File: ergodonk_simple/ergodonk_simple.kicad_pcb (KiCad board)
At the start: 2 copper layers, 216.6 x 155.6 mm, 134 parts, among them J10 Pimaroni Trackball, J11 4PIN, Q1 TIP120, SW0 SW_PUSH_LED, SW08_RH10 SW_PUSH_LED, SW1 SW_PUSH_LED, SW10 SW_PUSH_LED, SW11 SW_PUSH_LED, SW12 SW_PUSH_LED, SW13 SW_PUSH_LED, SW14 SW_PUSH_LED, SW15 SW_PUSH_LED, SW16 SW_PUSH_LED, SW17 SW_PUSH_LED, SW18_RH10 SW_PUSH_LED, SW2 SW_PUSH_LED, SW20 SW_PUSH_LED, SW21 SW_PUSH_LED, SW22 SW_PUSH_LED, SW23 SW_PUSH_LED, SW24 SW_PUSH_LED, SW25 SW_PUSH_LED, SW26 SW_PUSH_LED, SW27 SW_PUSH_LED, SW28_RH10 SW_PUSH_LED, SW3 SW_PUSH_LED, SW30 SW_PUSH_LED, SW31 SW_PUSH_LED, SW32 SW_PUSH_LED, SW33 SW_PUSH_LED, SW34 SW_PUSH_LED, SW35 SW_PUSH_LED, SW36 SW_PUSH_LED, SW37 SW_PUSH_LED, SW38_RH10 SW_PUSH_LED, SW4 SW_PUSH_LED, SW40 SW_PUSH_LED, SW42 SW_PUSH_LED, SW43 SW_PUSH_LED, SW44 SW_PUSH_LED, SW45 SW_PUSH_LED, SW46 SW_PUSH_LED, SW47 SW_PUSH_LED, SW48_RH10 SW_PUSH_LED, SW5 SW_PUSH_LED, SW50 SW_PUSH_LED, SW51 SW_PUSH_LED, SW52 SW_PUSH_LED, SW53 SW_PUSH_LED, SW54 SW_PUSH_LED, SW55 SW_PUSH_LED, SW56 SW_PUSH_LED, SW57 SW_PUSH_LED, SW58 SW_PUSH_LED, SW6 SW_PUSH_LED, SW7 SW_PUSH_LED, U11 Pico

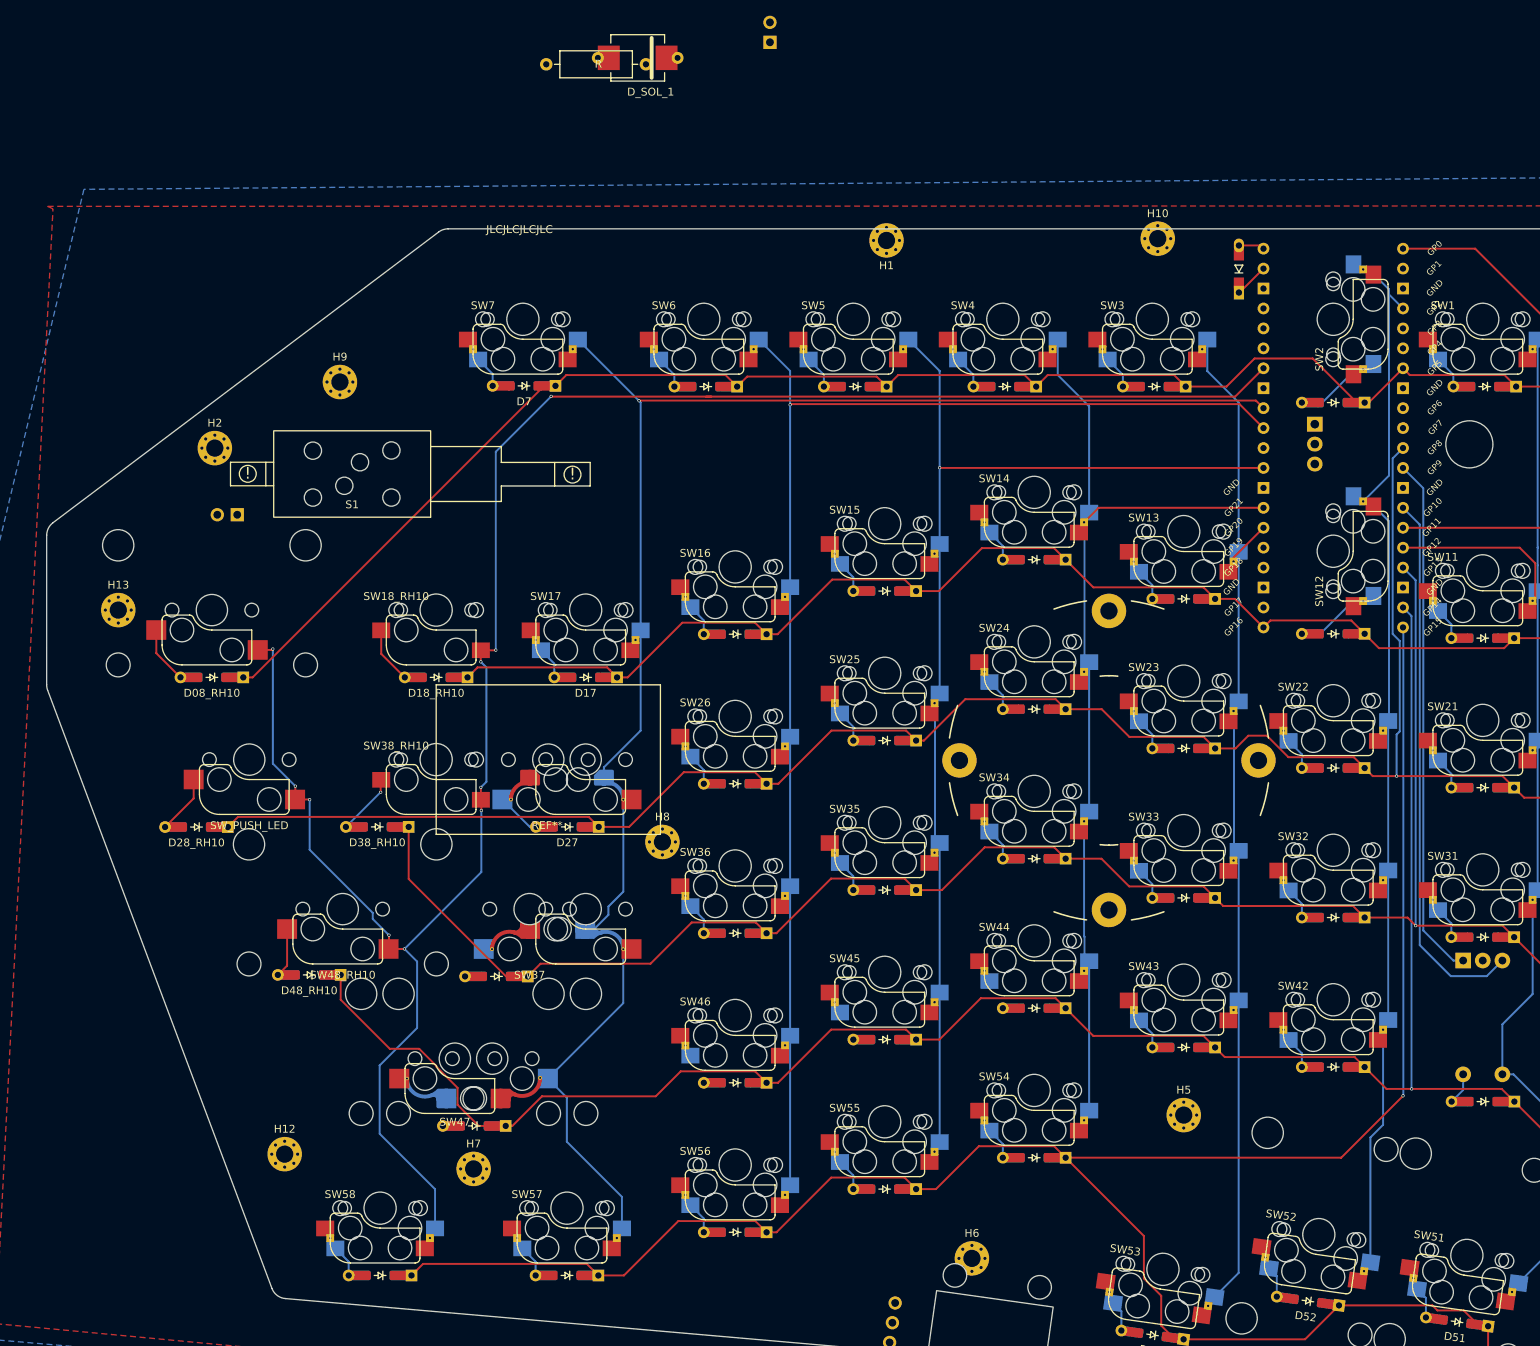
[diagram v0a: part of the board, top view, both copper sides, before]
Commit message: simple variant rh-brh-breakoff outline
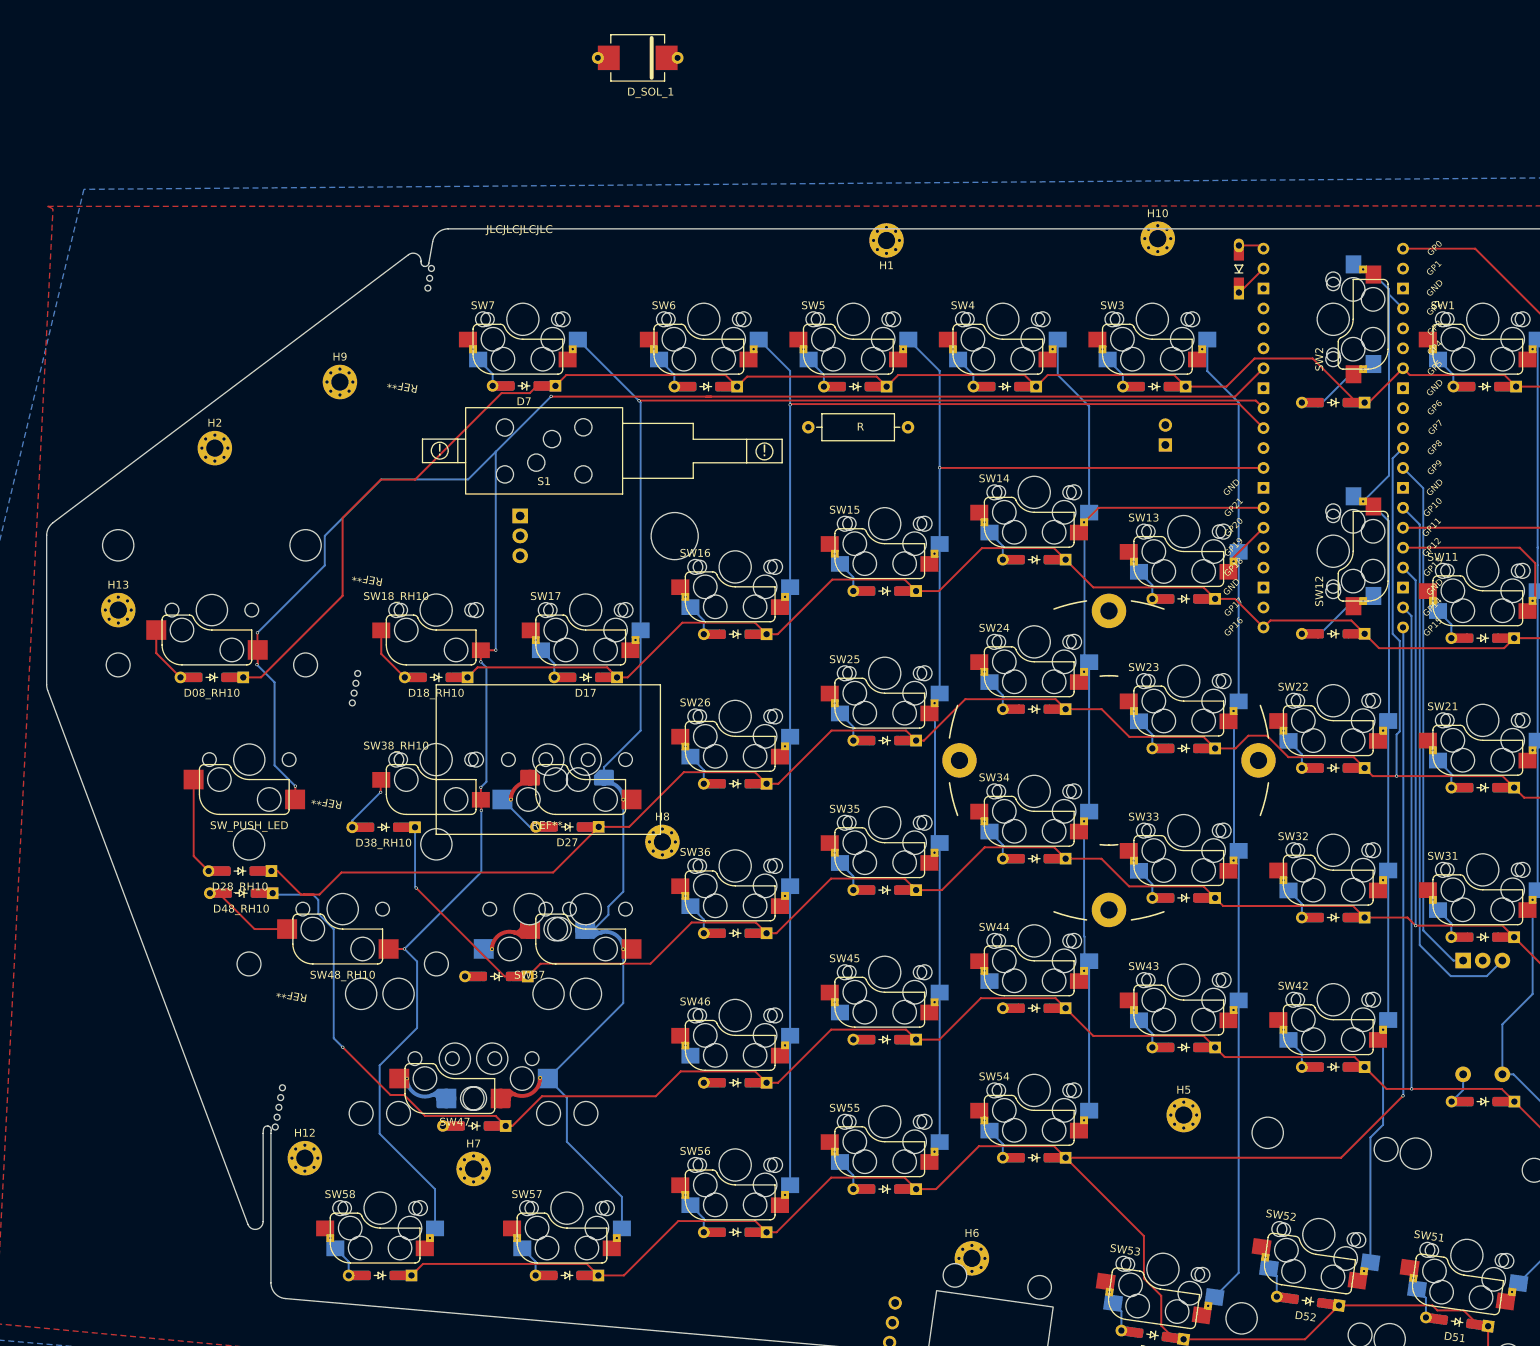
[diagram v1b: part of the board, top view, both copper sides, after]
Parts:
- removed JP3: LH LED's, Connector_PinHeader_2.54mm:PinHeader_1x02_P2.54mm_Vertical
- added REF**: mousebites 1mm, ergodonk_simple:mousebites_1mm_3up, F.Cu at (83.8, 28.6)
- added REF**: slot 24mm, ergodonk_simple:slot 24mm, F.Cu at (70.8, 94.9)
- added REF**: mousebites 1mm, ergodonk_simple:mousebites_1mm_4up, F.Cu at (74.3, 80.8)
- added REF**: slot 24mm, ergodonk_simple:slot 24mm, F.Cu at (80.5, 41.9)
- added REF**: slot 24mm, ergodonk_simple:slot 24mm, F.Cu at (76.0, 66.5)
- added REF**: mousebites 1mm, ergodonk_simple:mousebites_1mm_5up, F.Cu at (64.6, 134.2)
- added REF**: slot 24mm, ergodonk_simple:slot 24mm, F.Cu at (66.4, 119.5)
- moved Q1 101.9 mm to (106.6, 61.4)
- moved J_SOL_1 71.9 mm to (177.6, 49.8)
- moved R2 57.0 mm to (132.1, 47.6)
- moved S1 24.6 mm to (98.4, 50.6)
- moved D48_RH10 13.5 mm to (59.8, 106.9)
- moved D28_RH10 7.89 mm to (59.7, 104.1)
- moved H12 2.62 mm to (67.9, 140.7)
- moved D38_RH10 0.81 mm to (78.0, 98.5)
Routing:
- net row4: track 264.5 -> 284.8 mm, vias 1 -> 2
- net col8: track 263.5 -> 281.6 mm, vias 10 -> 9
- net row0: track 233.0 -> 237.9 mm
- net Net-(D28_RH10-A): track 7.56 -> 12.5 mm
- net Net-(D48_RH10-A): track 6.33 -> 10.6 mm
- net row3: track 244.1 -> 243.9 mm, vias 1 -> 2
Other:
- outline, holes or cut-outs redrawn
